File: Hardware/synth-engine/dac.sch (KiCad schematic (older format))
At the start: 17 parts

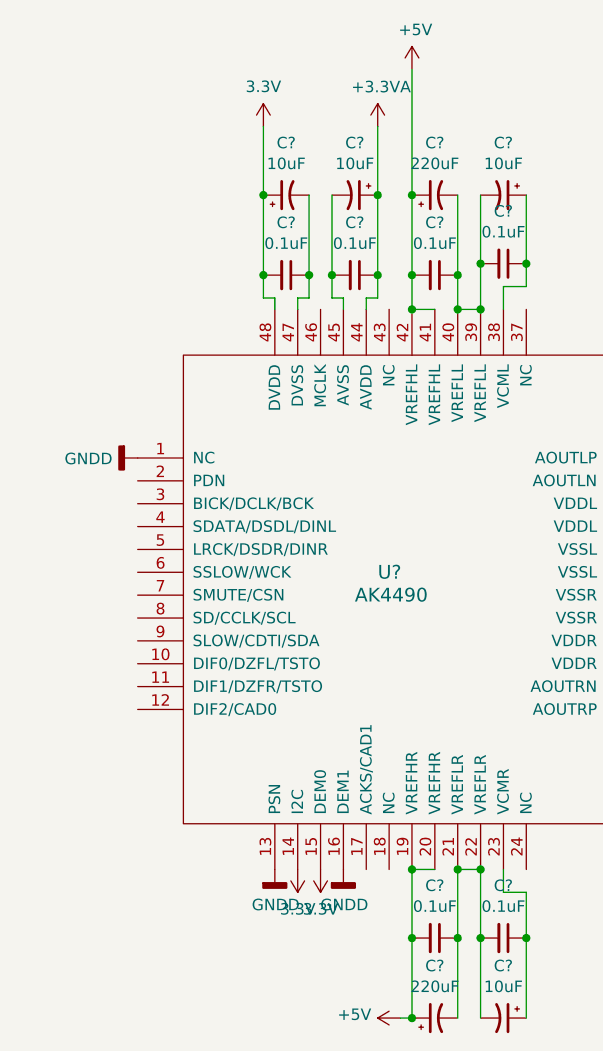
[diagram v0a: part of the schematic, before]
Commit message: add I/O connections between DAC and STM32 pages
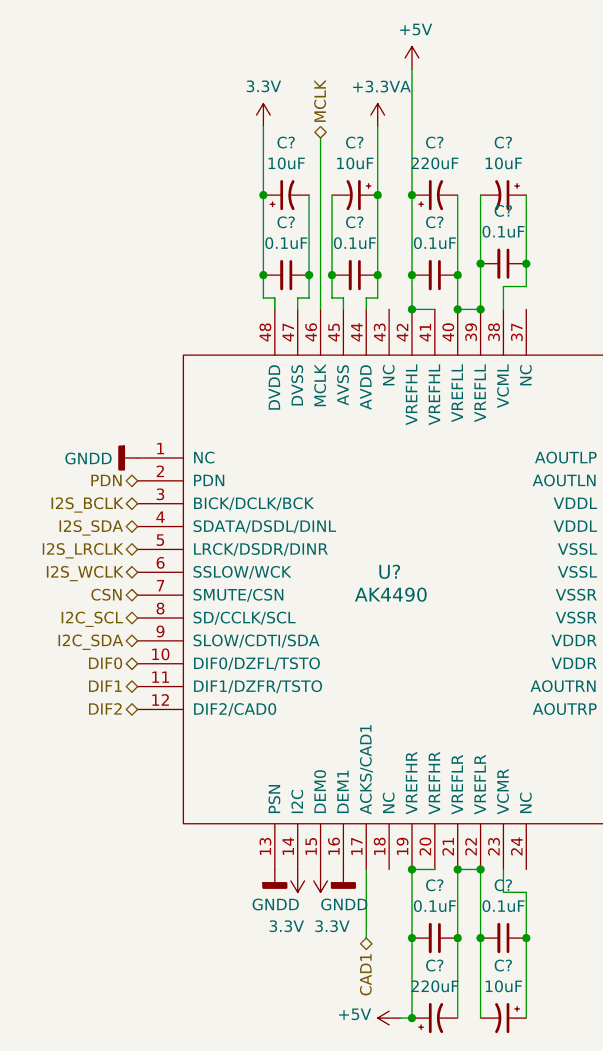
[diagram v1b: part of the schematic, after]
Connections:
- net DIF0: now reaches U?.10 (DIF0/DZFL/TSTO)
- net DIF1: now reaches U?.11 (DIF1/DZFR/TSTO)
- net DIF2: now reaches U?.12 (DIF2/CAD0)
- net CAD1: now reaches U?.17 (ACKS/CAD1)
- net PDN: now reaches U?.2 (PDN)
- net I2S_BCLK: now reaches U?.3 (BICK/DCLK/BCK)
- net I2S_SDA: now reaches U?.4 (SDATA/DSDL/DINL)
- net MCLK: now reaches U?.46 (MCLK)
- net I2S_LRCLK: now reaches U?.5 (LRCK/DSDR/DINR)
- net I2S_WCLK: now reaches U?.6 (SSLOW/WCK)
- net CSN: now reaches U?.7 (SMUTE/CSN)
- net I2C_SCL: now reaches U?.8 (SD/CCLK/SCL)
- net I2C_SDA: now reaches U?.9 (SLOW/CDTI/SDA)
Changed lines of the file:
@@
 P 4700 5300
 F 0 "#SUPPLY?" H 4700 5300 50  0001 L BNN
-F 1 "3.3V" H 4700 5474 50  0000 C CNN
+F 1 "3.3V" H 4750 5550 50  0000 C CNN
 F 2 "" H 4700 5300 50  0001 C CNN
 F 3 "" H 4700 5300 50  0001 C CNN
@@
 P 4800 5300
 F 0 "#SUPPLY?" H 4800 5300 50  0001 L BNN
-F 1 "3.3V" H 4800 5474 50  0000 C CNN
+F 1 "3.3V" H 4750 5550 50  0000 C CNN
 F 2 "" H 4800 5300 50  0001 C CNN
 F 3 "" H 4800 5300 50  0001 C CNN
@@
 	-1   0    0    1
 $EndComp
+Text HLabel 4800 2100 1    50   BiDi ~ 0
+MCLK
+Wire Wire Line
+	4800 2100 4800 2850
+Text HLabel 4000 3600 0    50   BiDi ~ 0
+PDN
+Text HLabel 4000 3700 0    50   BiDi ~ 0
+I2S_BCLK
+Text HLabel 4000 3800 0    50   BiDi ~ 0
+I2S_SDA
+Text HLabel 4000 3900 0    50   BiDi ~ 0
+I2S_LRCLK
+Text HLabel 4000 4000 0    50   BiDi ~ 0
+I2S_WCLK
+Text HLabel 4000 4100 0    50   BiDi ~ 0
+CSN
+Text HLabel 4000 4200 0    50   BiDi ~ 0
+I2C_SCL
+Text HLabel 4000 4300 0    50   BiDi ~ 0
+I2C_SDA
+Text HLabel 4000 4400 0    50   BiDi ~ 0
+DIF0
+Text HLabel 4000 4500 0    50   BiDi ~ 0
+DIF1
+Text HLabel 4000 4600 0    50   BiDi ~ 0
+DIF2
+Text HLabel 5000 5600 3    50   BiDi ~ 0
+CAD1
+Wire Wire Line
+	5000 5600 5000 5300
 $EndSCHEMATC

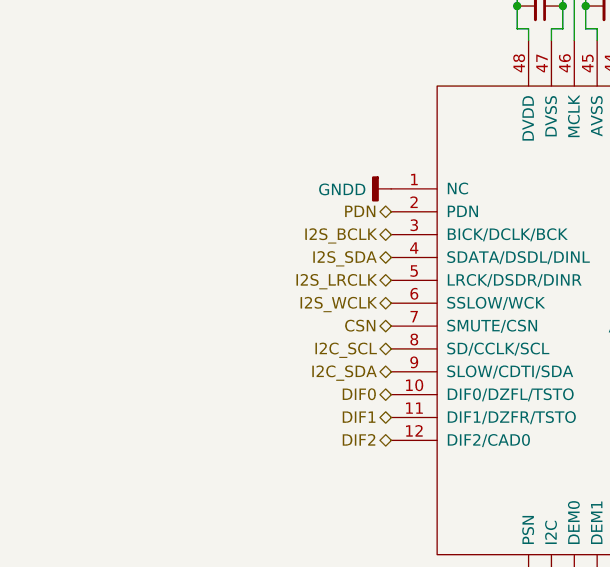
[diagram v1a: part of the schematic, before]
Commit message: add pullup resistors to I2C lines
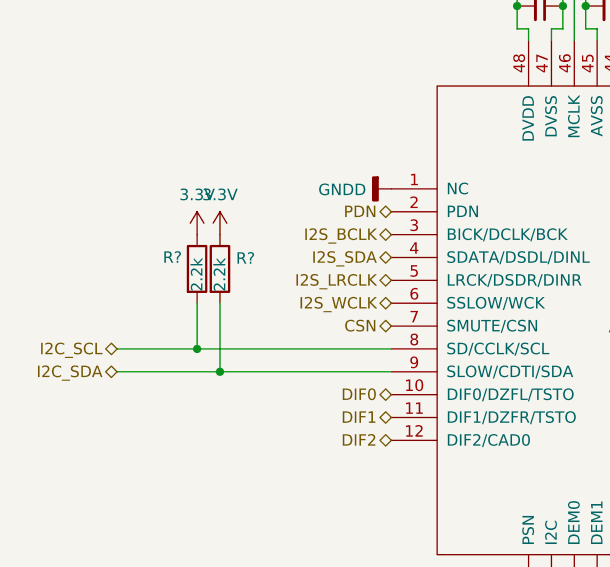
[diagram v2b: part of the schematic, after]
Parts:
- added R? (x2): 2.2k, symbol Device:R
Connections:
- net 3.3V: now also R?.1, R?.1
- net I2C_SCL: now also R?.2
- net I2C_SDA: now also R?.2
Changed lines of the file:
@@
 Text HLabel 4000 4100 0    50   BiDi ~ 0
 CSN
-Text HLabel 4000 4200 0    50   BiDi ~ 0
+Text HLabel 2800 4200 0    50   BiDi ~ 0
 I2C_SCL
-Text HLabel 4000 4300 0    50   BiDi ~ 0
+Text HLabel 2800 4300 0    50   BiDi ~ 0
 I2C_SDA
 Text HLabel 4000 4400 0    50   BiDi ~ 0
@@
 Wire Wire Line
 	5000 5600 5000 5300
+$Comp
+L Device:R R?
+U 1 1 5DD990DD
+P 3150 3850
+F 0 "R?" H 3000 3900 50  0000 L CNN
+F 1 "2.2k" V 3150 3750 50  0000 L CNN
+F 2 "" V 3080 3850 50  0001 C CNN
+F 3 "~" H 3150 3850 50  0001 C CNN
+	1    3150 3850
+	1    0    0    -1
+$EndComp
+$Comp
+L Device:R R?
+U 1 1 5DD99194
+P 3250 3850
+F 0 "R?" H 3320 3896 50  0000 L CNN
+F 1 "2.2k" V 3250 3750 50  0000 L CNN
+F 2 "" V 3180 3850 50  0001 C CNN
+F 3 "~" H 3250 3850 50  0001 C CNN
+	1    3250 3850
+	1    0    0    -1
+$EndComp
+$Comp
+L SparkFun-Aesthetics:3.3V #SUPPLY?
+U 1 1 5DD9B51B
+P 3250 3700
+F 0 "#SUPPLY?" H 3250 3700 50  0001 L BNN
+F 1 "3.3V" H 3250 3874 50  0000 C CNN
+F 2 "" H 3250 3700 50  0001 C CNN
+F 3 "" H 3250 3700 50  0001 C CNN
+	1    3250 3700
+	1    0    0    -1
+$EndComp
+$Comp
+L SparkFun-Aesthetics:3.3V #SUPPLY?
+U 1 1 5DD9B54C
+P 3150 3700
+F 0 "#SUPPLY?" H 3150 3700 50  0001 L BNN
+F 1 "3.3V" H 3150 3874 50  0000 C CNN
+F 2 "" H 3150 3700 50  0001 C CNN
+F 3 "" H 3150 3700 50  0001 C CNN
+	1    3150 3700
+	1    0    0    -1
+$EndComp
+Wire Wire Line
+	2800 4200 3150 4200
+Wire Wire Line
+	2800 4300 3250 4300
+Wire Wire Line
+	3150 4000 3150 4200
+Connection ~ 3150 4200
+Wire Wire Line
+	3150 4200 4000 4200
+Wire Wire Line
+	3250 4000 3250 4300
+Connection ~ 3250 4300
+Wire Wire Line
+	3250 4300 4000 4300
 $EndSCHEMATC

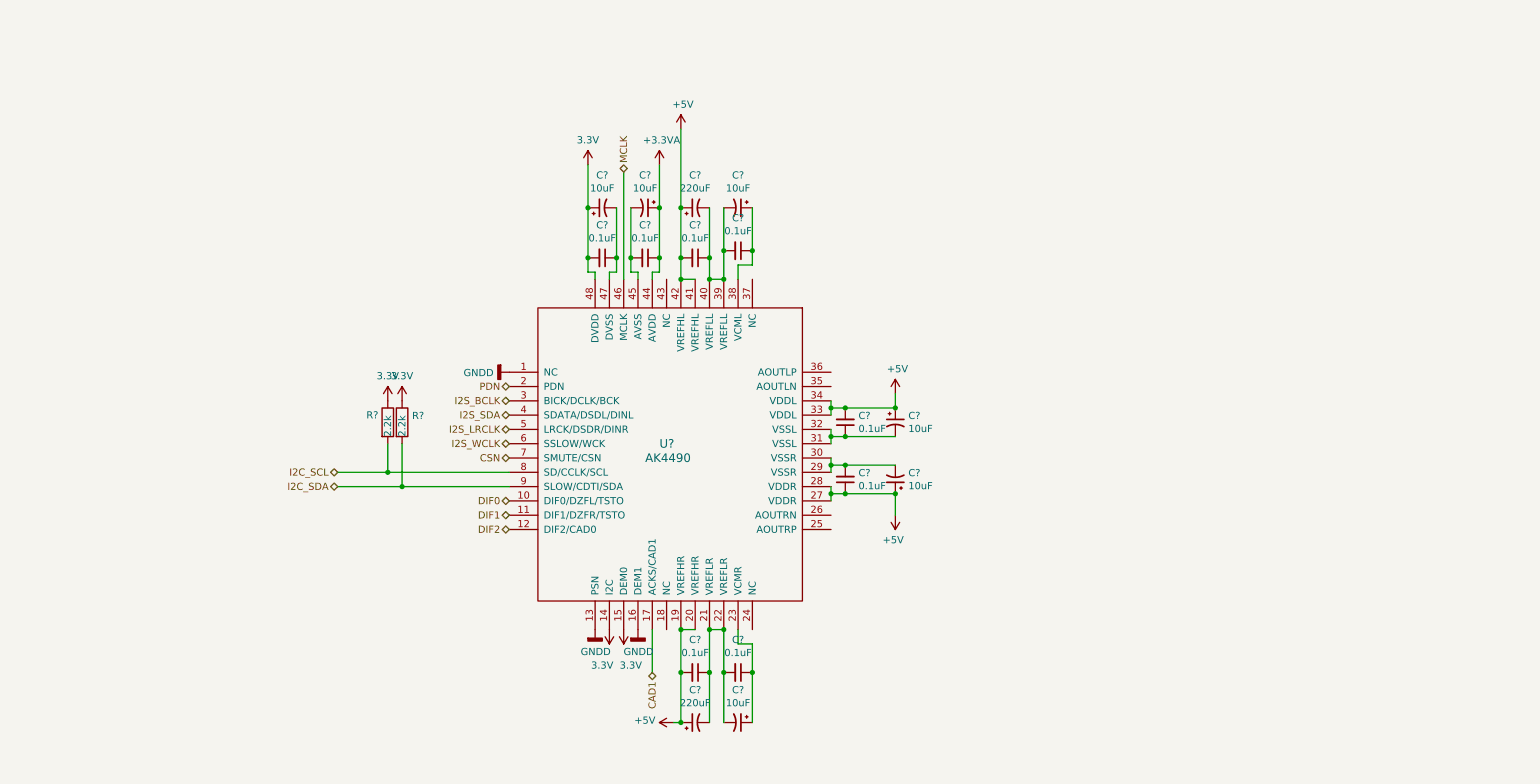
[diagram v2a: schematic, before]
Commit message: add missing ground connections to AK4490 Probably need to double check all the grounding on this again.
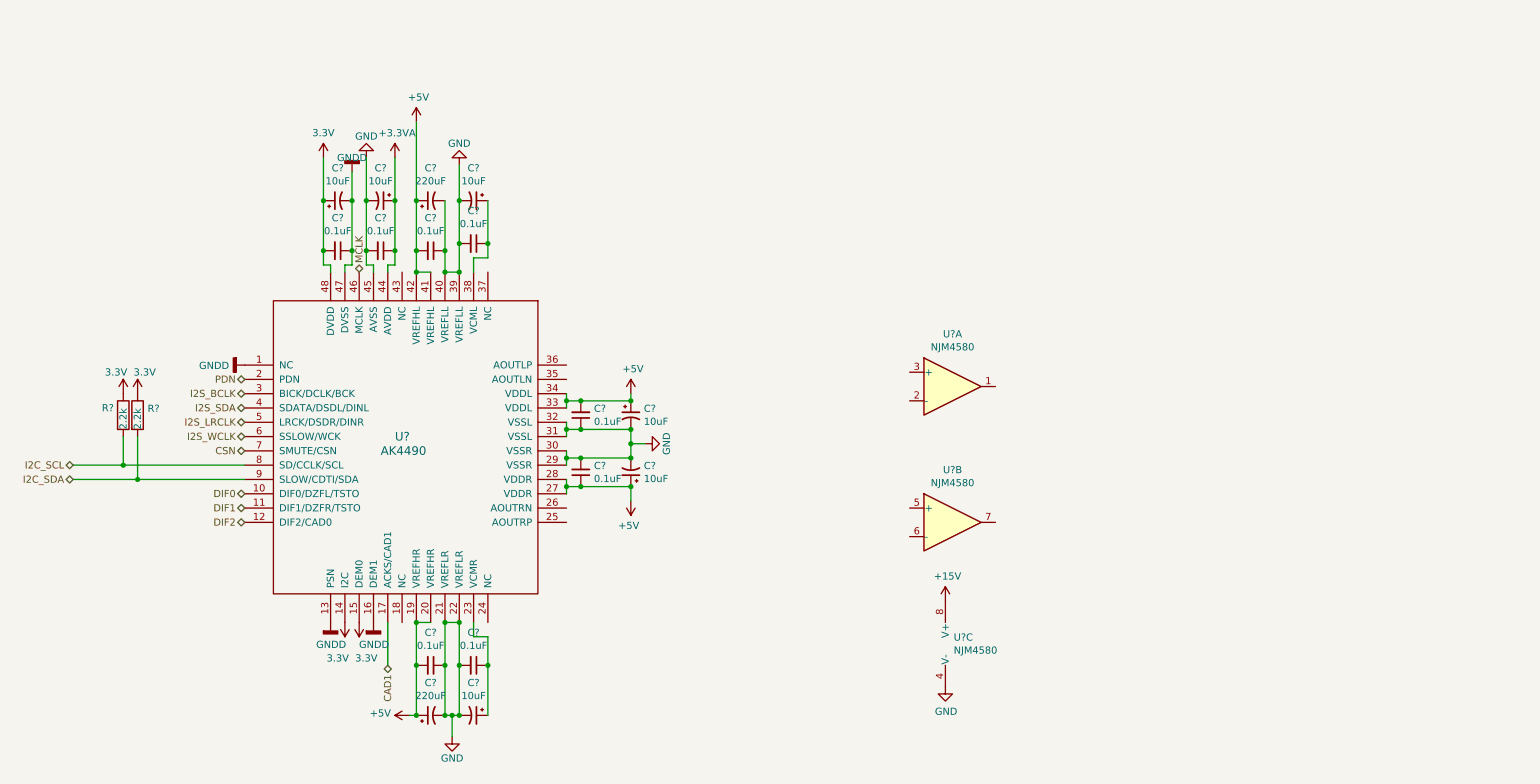
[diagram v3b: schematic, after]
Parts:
- added U? (x3): NJM4580, symbol Amplifier_Operational:NJM4580
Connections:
- net GNDD: now also C?.1, C?.2, U?.47 (DVSS)
- net GND: now reaches C?.1, C?.2, C?.2, C?.2, U?.21 (VREFLR), U?.22 (VREFLR)
- net GND: now also C?.1, C?.1, C?.2, C?.2, C?.2, C?.2, C?.2, C?.2, C?.2, C?.2, U?.29 (VSSR), U?.30 (VSSR), U?.31 (VSSL), U?.32 (VSSL), U?.39 (VREFLL), U?.40 (VREFLL), U?.45 (AVSS), U?.4 (V-)
- new net +15V: U?.8 (V+)
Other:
- moved on the sheet: C?, R?, U?

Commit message: add LFP following DAC diff outputs and connect DAC output to VCF input
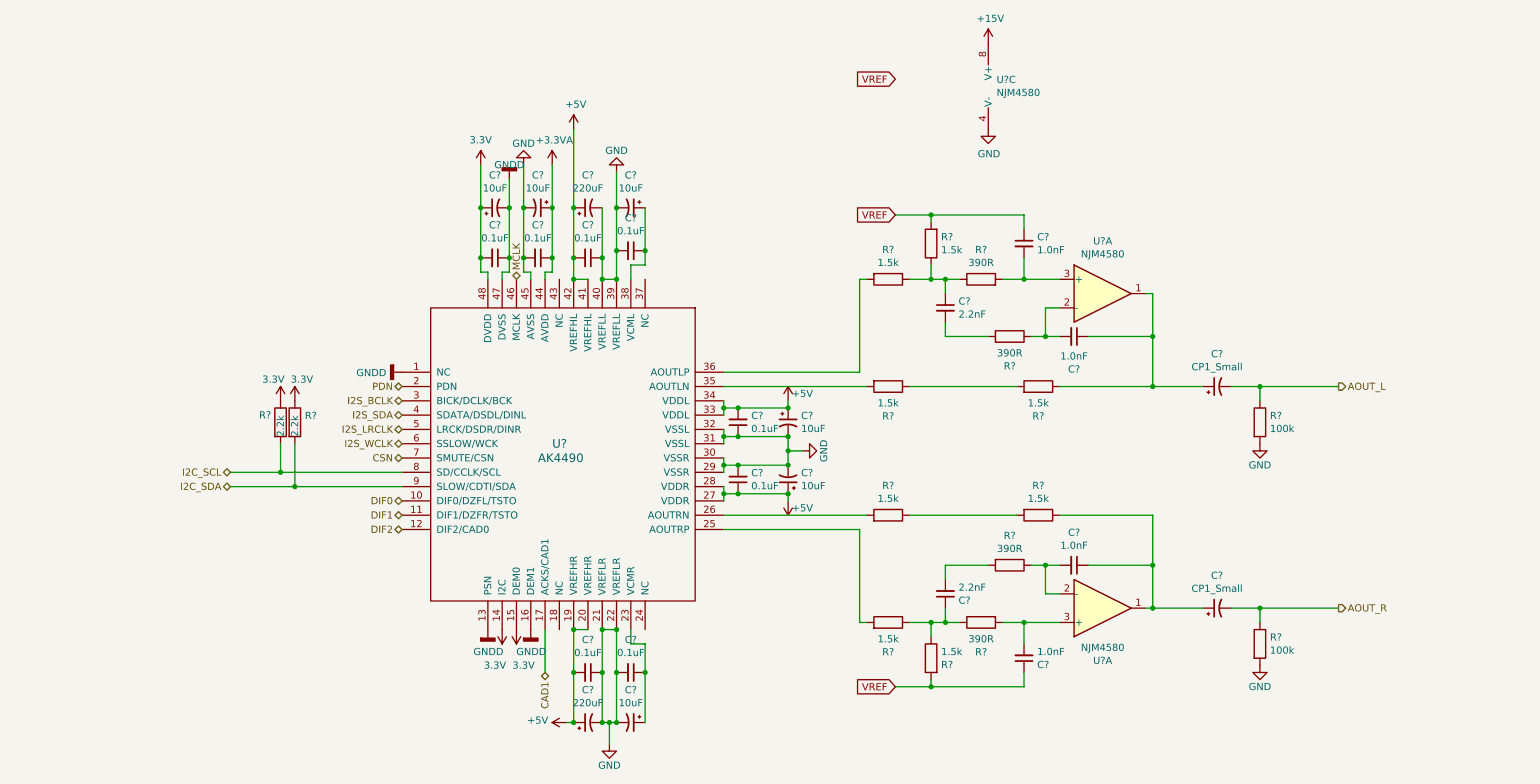
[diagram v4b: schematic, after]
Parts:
- removed U?: NJM4580, symbol Amplifier_Operational:NJM4580
- added C? (x4): 1.0nF, symbol Device:C_Small
- added C? (x2): 2.2nF, symbol Device:C_Small
- added C? (x2): CP1_Small, symbol Device:CP1_Small
- added R? (x8): 1.5k, symbol Device:R
- added R? (x4): 390R, symbol Device:R
- added R? (x2): 100k, symbol Device:R
- added U?: NJM4580, symbol Amplifier_Operational:NJM4580
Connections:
- net GND: now also R?.2, R?.2
- net at U?.25 (AOUTRP): now also R?.2
- net at U?.26 (AOUTRN): now also R?.2
- net at U?.35 (AOUTLN): now also R?.2
- net at U?.36 (AOUTLP): now also R?.2
- net at U?.1: now also C?.1, C?.1, R?.1
- net at U?.2 (-): now also C?.2, R?.1
- net at U?.3 (+): now also C?.2, R?.2
- new net: C?.1, R?.1, R?.1, R?.1 (x2)
- new net: C?.2, R?.2 (x2)
- new net: R?.1, R?.2 (x2)
- new net: C?.1, C?.1, R?.1, U?.1
- new net: C?.2, R?.1, U?.2 (-)
- new net: C?.2, R?.2, U?.3 (+)
- new net AOUT_L: C?.2, R?.1
- new net AOUT_R: C?.2, R?.1
- new net VREF: C?.1, C?.1, R?.2, R?.2
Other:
- moved on the sheet: C?, R?, U?, U?A, U?C

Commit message: add filtering in front of 3.3V regulators
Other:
- note added: "I think I could DC couple this\nand remove coupling caps\nbecause filters will be biased\nto the same VREF (?)"
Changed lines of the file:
@@
 	9800 5150 9250 5150
 Connection ~ 9250 5150
+Text Notes 9650 4200 0    50   ~ 0
+I think I  could DC couple this\nand remove coupling caps\nbecause filters will be biased\nto the same VREF (?)
 $EndSCHEMATC

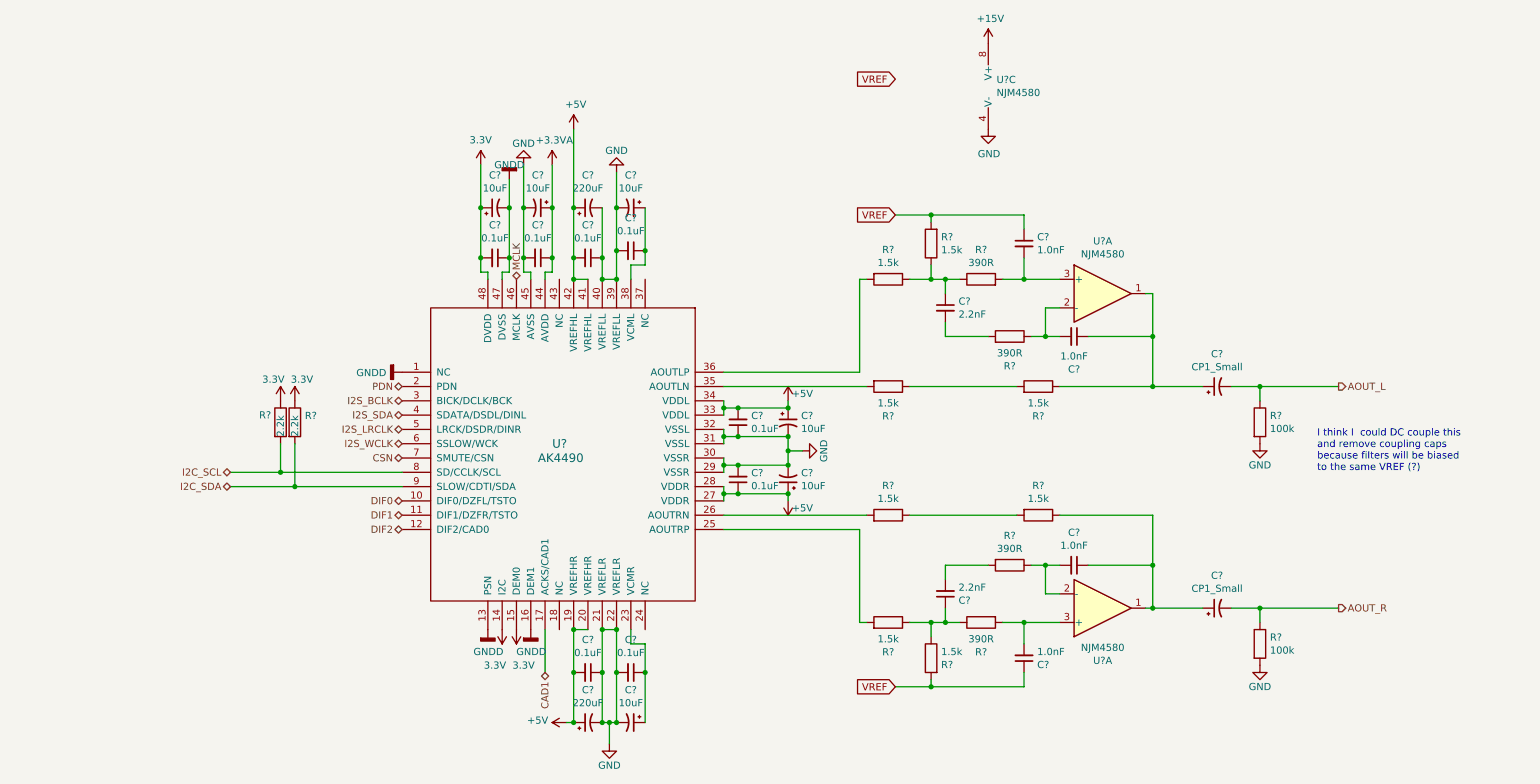
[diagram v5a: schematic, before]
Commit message: assign footprints to schematic symbols.
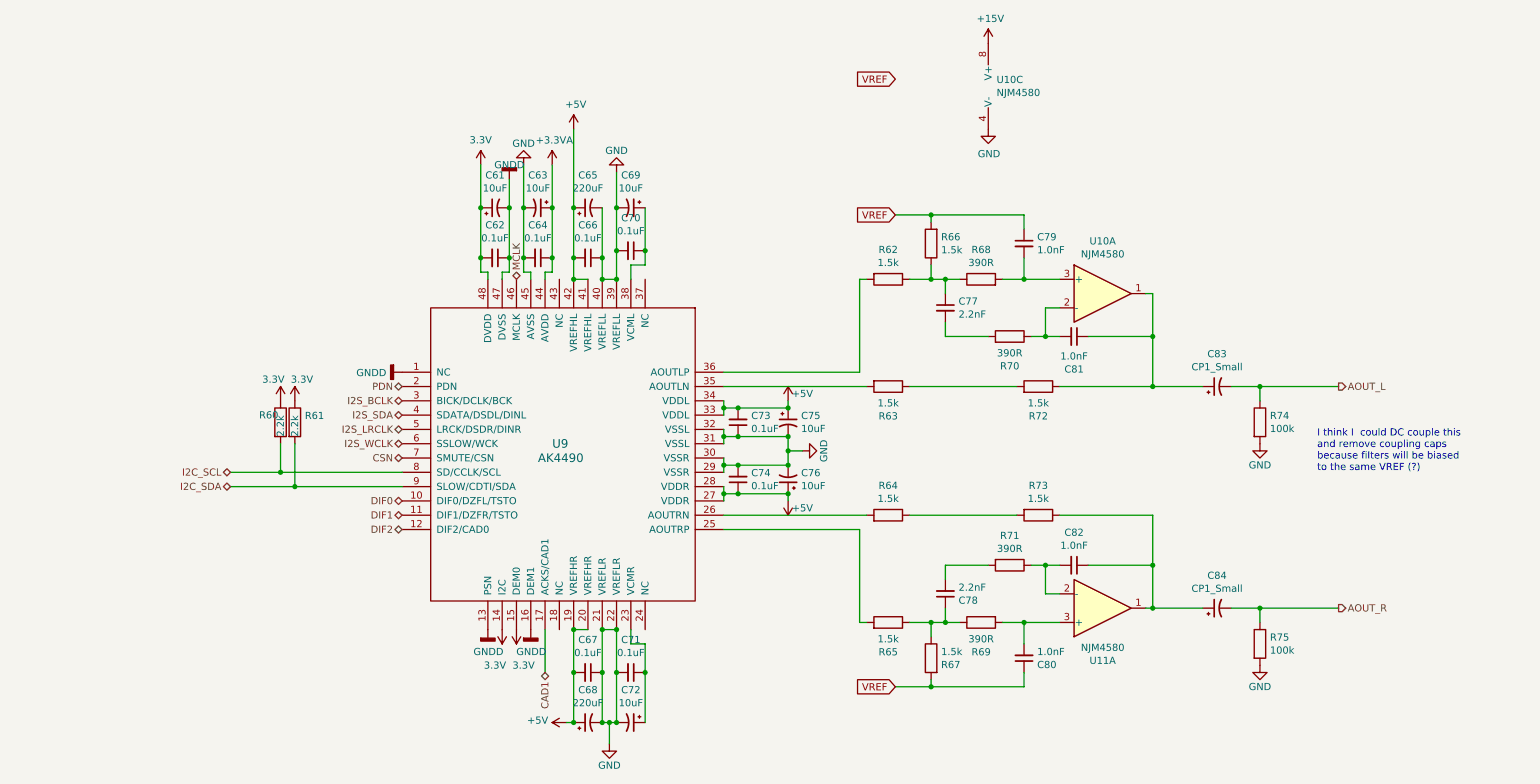
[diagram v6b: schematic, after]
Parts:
- C61, C63, C65, C68, C69, C72, C75, C76, C83, C84: renamed from C?; footprint (none) -> Capacitor_SMD:CP_Elec_6.3x5.4
- C62, C64, C66, C67, C70, C71, C73, C74, C77, C78, C79, C80, C81, C82: renamed from C?; footprint (none) -> SparkFun-Passives:0805
- R60, R61, R62, R63, R64, R65, R66, R67, R68, R69, R70, R71, R72, R73, R74, R75: renamed from R?; footprint (none) -> SparkFun-Passives:0805
- U10, U11: renamed from U?; footprint (none) -> SparkFun-DigitalIC:SO08
- U9: renamed from U?; footprint (none) -> SparkFun-DigitalIC:LQFP-48
